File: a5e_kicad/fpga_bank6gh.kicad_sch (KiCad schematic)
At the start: 1 part, among them U7 A5EB013B-B23B

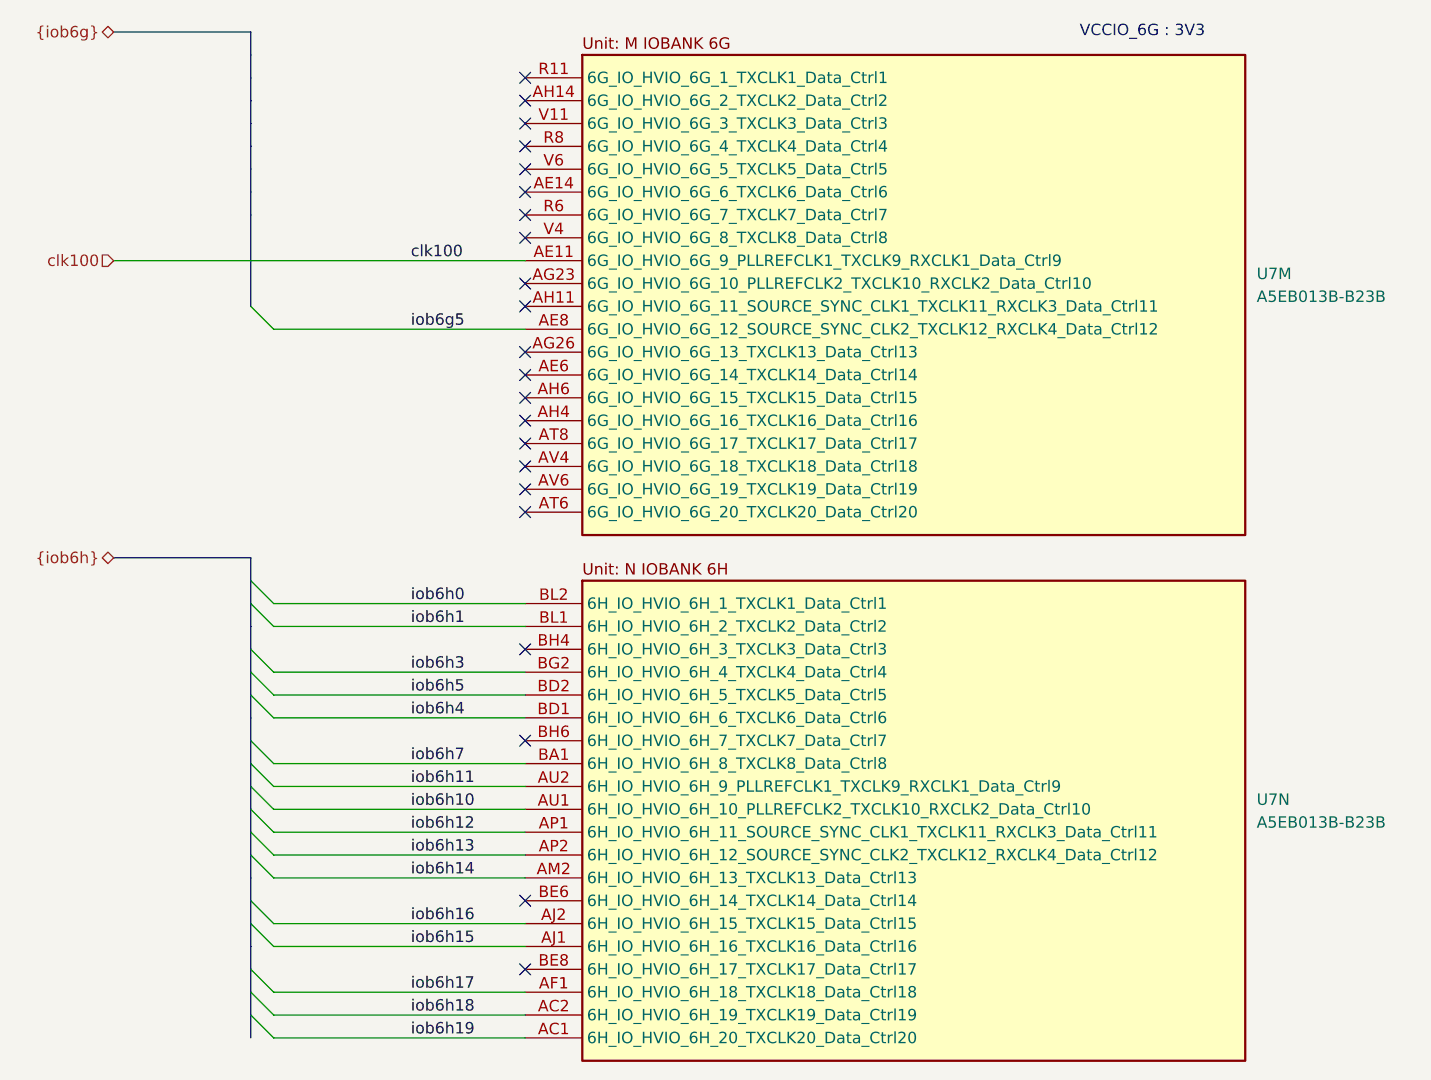
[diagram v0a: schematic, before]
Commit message: Ethernet PHY passives to 0201, R27/R28 to 0402, preliminary RGMII routing
- 31 PHY passives on the hps_ethernet sheet 0402 -> 0201 (C24 22u stays
  0402): 100n C190183, 1u C272877, 27p C85899, 10k C473048,
  330R C516485, 4K7 C270346, 1K5 C270361, 2K49 C473476.
- Refclk bias R27/R28 0201 -> 0402 (C25120, 49.9R); R28 moved 0.1 mm
  to +x to clear the refclk_N meander.
- Preliminary RGMII routing: RX on F.Cu, TX on In2. Group spread
  TX 79 ps (TXD1 longest), RX 44 ps.
- Schematic sheets as saved by eeschema.
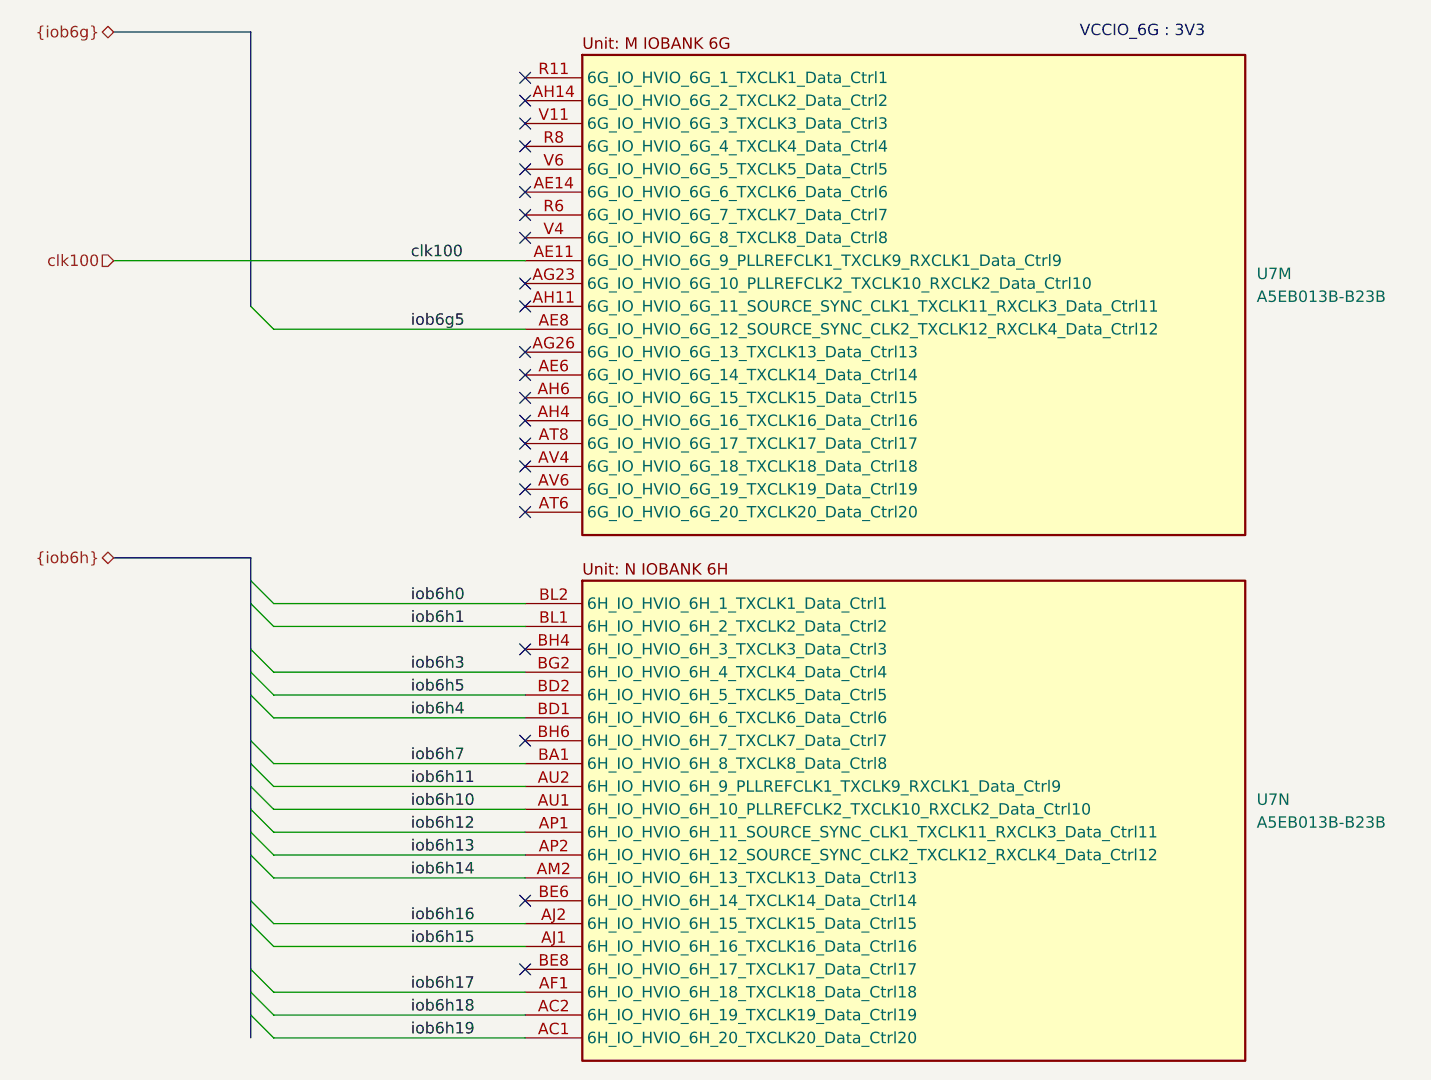
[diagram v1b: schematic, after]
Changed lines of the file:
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@@
 	)
 	(no_connect
+		(at 96.52 119.38)
+	)
+	(no_connect
 		(at 96.52 76.2)
 	)
@@
 	)
 	(no_connect
+		(at 96.52 127)
+	)
+	(no_connect
+		(at 96.52 43.18)
+	)
+	(no_connect
+		(at 96.52 45.72)
+	)
+	(no_connect
+		(at 96.52 101.6)
+	)
+	(no_connect
+		(at 96.52 40.64)
+	)
+	(no_connect
 		(at 96.52 53.34)
 	)
@@
 	)
 	(no_connect
+		(at 96.52 35.56)
+	)
+	(no_connect
+		(at 96.52 38.1)
+	)
+	(no_connect
 		(at 96.52 71.12)
 	)
 	(no_connect
+		(at 96.52 33.02)
+	)
+	(no_connect
+		(at 96.52 30.48)
+	)
+	(no_connect
 		(at 96.52 50.8)
 	)
 	(no_connect
+		(at 96.52 27.94)
+	)
+	(no_connect
 		(at 96.52 63.5)
 	)
+	(no_connect
+		(at 96.52 91.44)
+	)
 	(bus_entry
 		(at 66.04 121.92)
@@
 	(bus
 		(pts
-			(xy 66.04 27.94) (xy 66.04 30.48)
-		)
-		(stroke
-			(width 0)
-			(type default)
-		)
-	)
-	(bus
-		(pts
 			(xy 50.8 22.86) (xy 66.04 22.86)
 		)
@@
 	(bus
 		(pts
-			(xy 66.04 116.84) (xy 66.04 119.38)
+			(xy 66.04 114.3) (xy 66.04 119.38)
 		)
 		(stroke
@@
 		)
 	)
-	(bus
-		(pts
-			(xy 66.04 33.02) (xy 66.04 35.56)
-		)
-		(stroke
-			(width 0)
-			(type default)
-		)
-	)
-	(bus
-		(pts
-			(xy 66.04 40.64) (xy 66.04 43.18)
-		)
-		(stroke
-			(width 0)
-			(type default)
-		)
-	)
 	(wire
 		(pts
@@
 	(bus
 		(pts
-			(xy 66.04 38.1) (xy 66.04 40.64)
+			(xy 66.04 22.86) (xy 66.04 53.34)
 		)
 		(stroke
@@
 		)
 	)
-	(bus
-		(pts
-			(xy 66.04 114.3) (xy 66.04 116.84)
-		)
-		(stroke
-			(width 0)
-			(type default)
-		)
-	)
 	(wire
 		(pts
@@
 		)
 	)
-	(bus
-		(pts
-			(xy 66.04 43.18) (xy 66.04 53.34)
-		)
-		(stroke
-			(width 0)
-			(type default)
-		)
-	)
 	(wire
 		(pts
@@
 	(bus
 		(pts
-			(xy 66.04 121.92) (xy 66.04 124.46)
+			(xy 66.04 121.92) (xy 66.04 127)
 		)
 		(stroke
@@
 		)
 	)
-	(bus
-		(pts
-			(xy 66.04 124.46) (xy 66.04 127)
-		)
-		(stroke
-			(width 0)
-			(type default)
-		)
-	)
-	(bus
-		(pts
-			(xy 66.04 88.9) (xy 66.04 91.44)
-		)
-		(stroke
-			(width 0)
-			(type default)
-		)
-	)
 	(wire
 		(pts
@@
 	(bus
 		(pts
-			(xy 66.04 99.06) (xy 66.04 101.6)
+			(xy 66.04 96.52) (xy 66.04 101.6)
 		)
 		(stroke
@@
 	(bus
 		(pts
-			(xy 66.04 25.4) (xy 66.04 27.94)
-		)
-		(stroke
-			(width 0)
-			(type default)
-		)
-	)
-	(bus
-		(pts
 			(xy 66.04 132.08) (xy 66.04 134.62)
 		)
@@
 		)
 	)
-	(bus
-		(pts
-			(xy 66.04 22.86) (xy 66.04 25.4)
-		)
-		(stroke
-			(width 0)
-			(type default)
-		)
-	)
 	(wire
 		(pts
@@
 	(bus
 		(pts
-			(xy 66.04 30.48) (xy 66.04 33.02)
-		)
-		(stroke
-			(width 0)
-			(type default)
-		)
-	)
-	(bus
-		(pts
-			(xy 66.04 96.52) (xy 66.04 99.06)
-		)
-		(stroke
-			(width 0)
-			(type default)
-		)
-	)
-	(bus
-		(pts
-			(xy 66.04 86.36) (xy 66.04 88.9)
-		)
-		(stroke
-			(width 0)
-			(type default)
-		)
-	)
-	(bus
-		(pts
-			(xy 66.04 35.56) (xy 66.04 38.1)
+			(xy 66.04 86.36) (xy 66.04 91.44)
 		)
 		(stroke
@@
 		)
 	)
-	(no_connect
-		(at 96.52 119.38)
-	)
-	(no_connect
-		(at 96.52 33.02)
-	)
-	(no_connect
-		(at 96.52 127)
-	)
-	(no_connect
-		(at 96.52 45.72)
-	)
-	(no_connect
-		(at 96.52 101.6)
-	)
-	(no_connect
-		(at 96.52 35.56)
-	)
-	(no_connect
-		(at 96.52 30.48)
-	)
-	(no_connect
-		(at 96.52 27.94)
-	)
-	(no_connect
-		(at 96.52 40.64)
-	)
-	(no_connect
-		(at 96.52 38.1)
-	)
-	(no_connect
-		(at 96.52 43.18)
-	)
-	(no_connect
-		(at 96.52 91.44)
-	)
 )
